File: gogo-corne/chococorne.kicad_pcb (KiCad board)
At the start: 2 copper layers, 112.9 x 97.1 mm, 40 parts, among them J1 MJ-4PP-9, SW10 SW_PUSH, SW11 SW_PUSH, SW12 SW_PUSH, SW14 SW_PUSH, SW15 SW_PUSH, SW16 SW_PUSH, SW17 SW_PUSH, SW18 SW_PUSH, SW19 SW_PUSH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

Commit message: the neatening
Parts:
- moved D6 4.07 mm to (149.1, 71.6)
- moved D18 4.07 mm to (149.1, 93.2)
- moved D12 4.07 mm to (149.1, 81.8)
- moved D5 1.55 mm to (149.1, 58.9)
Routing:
- net row3: track 115.5 -> 150.9 mm
- net col1: track 163.8 -> 156.1 mm
- net row1: track 120.8 -> 127.0 mm
- net Net-(D18-Pad2): track 23.6 -> 18.8 mm
- net Net-(D17-Pad2): track 35.4 -> 38.4 mm
- net Net-(D6-Pad2): track 21.4 -> 24.0 mm
- net Net-(D11-Pad2): track 35.4 -> 37.9 mm
- net row2: track 112.4 -> 113.8 mm
- net row0: track 126.8 -> 128.2 mm
- net Net-(D19-Pad2): track 51.6 -> 50.6 mm
- net col3: track 128.1 -> 127.5 mm
- net col4: track 115.7 -> 115.2 mm

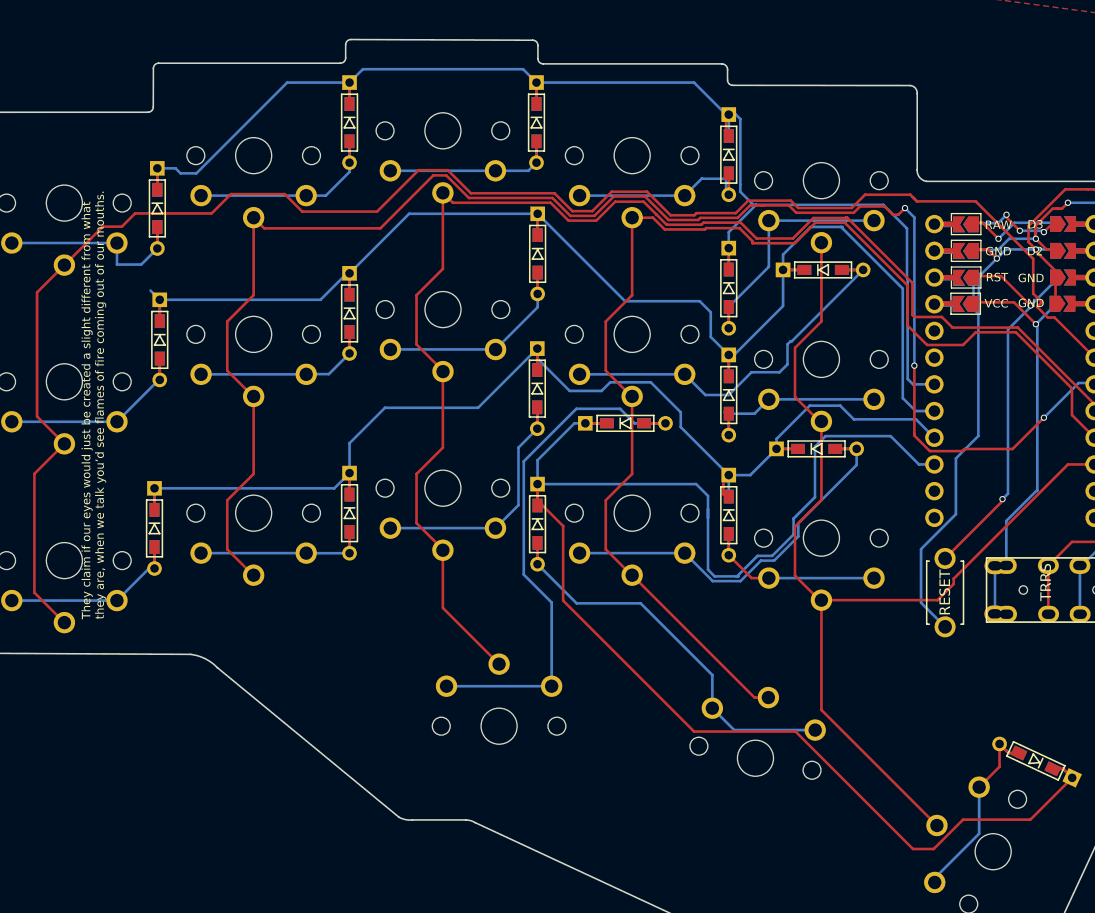
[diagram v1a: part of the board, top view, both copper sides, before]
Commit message: move some diodes
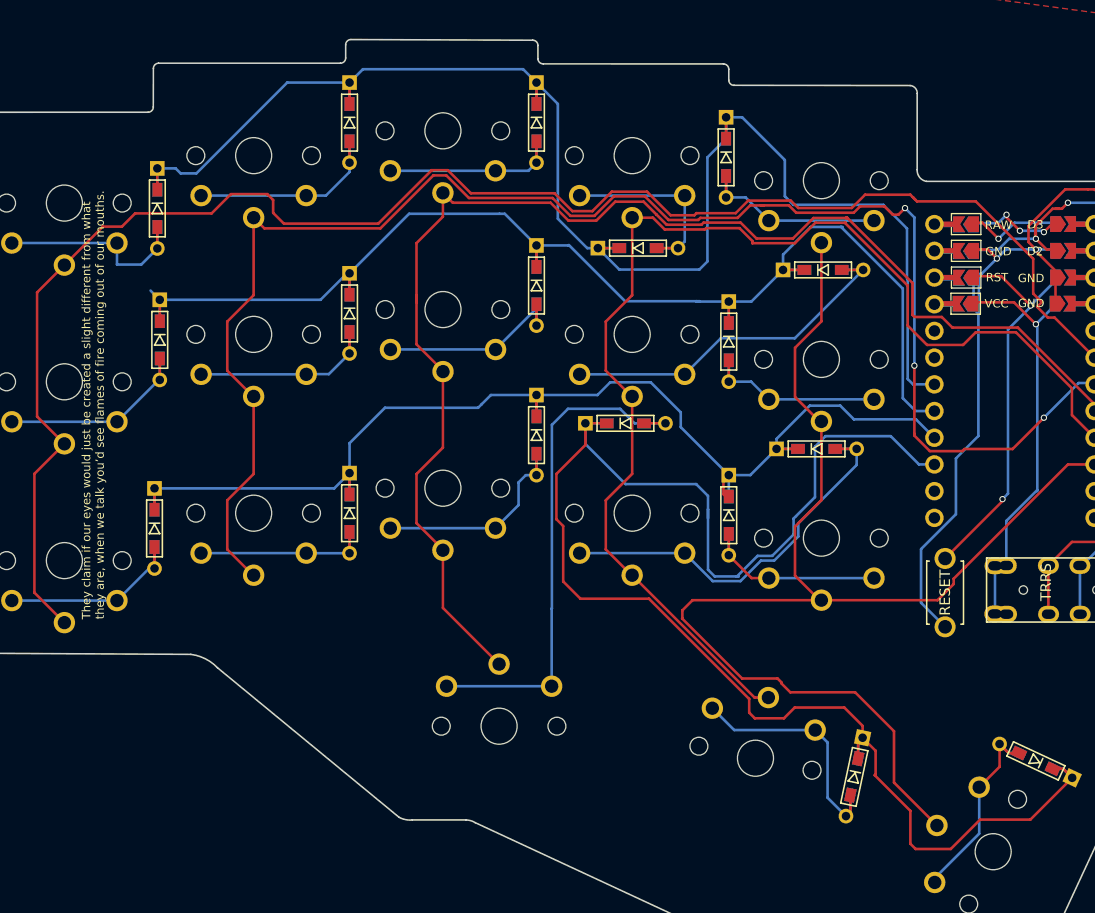
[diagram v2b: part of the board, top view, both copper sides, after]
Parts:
- moved D20 38.5 mm to (161.0, 118.1), turned to -102 degrees
- moved D6 12.4 mm to (148.8, 59.2)
- moved D5 12.4 mm to (140.5, 67.8), turned to 0 degrees
- moved D12 5.08 mm to (149.1, 76.7)
- moved D16 4.42 mm to (130.8, 85.6)
- moved D10 3.02 mm to (130.8, 71.4)
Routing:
- net col5: track 95.8 -> 119.5 mm
- net row0: track 128.2 -> 144.5 mm
- net Net-(D20-Pad2): track 38.9 -> 24.4 mm
- net row1: track 127.0 -> 119.8 mm
- net Net-(D6-Pad2): track 24.0 -> 19.2 mm
- net row2: track 113.8 -> 109.9 mm
- net Net-(D16-Pad2): track 25.2 -> 21.3 mm
- net Net-(D11-Pad2): track 37.9 -> 35.2 mm
- net Net-(D19-Pad2): track 50.6 -> 48.9 mm
- net col1: track 156.1 -> 157.8 mm
- net row3: track 150.9 -> 152.5 mm
- net Net-(D10-Pad2): track 21.0 -> 19.7 mm
- net Net-(D5-Pad2): track 18.6 -> 19.3 mm
- net col3: track 127.5 -> 128.1 mm
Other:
- outline, holes or cut-outs redrawn

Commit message: changes based on kyek's feedback
changes from @duckyb
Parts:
- SW10, SW11, SW12, SW14, SW15, SW16, SW17, SW18, SW19, SW2, SW3, SW4, SW5, SW6, SW8, SW9: footprint Kailh:SW_PG1350_rev_DPB2.2 -> Kailh:SW_PG1350_rev_DPB-mm
- moved D21 1.01 mm to (179.0, 115.8), turned to -25 degrees
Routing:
- net row3: track 152.5 -> 140.4 mm
- net Net-(D21-Pad2): track 20.1 -> 25.4 mm
- net col2: track 150.8 -> 152.5 mm
- net col1: track 157.8 -> 158.6 mm

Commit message: Fix DRC on gogo-corne
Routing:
- net col2: track 152.5 -> 142.1 mm
- net row1: track 119.8 -> 114.9 mm
- net row3: track 140.4 -> 136.0 mm
- net GND: track 113.2 -> 115.6 mm
- net Net-(D2-Pad2): track 20.6 -> 18.1 mm
- net row2: track 110.2 -> 112.2 mm
- net Net-(D19-Pad2): track 48.9 -> 50.0 mm
- net col5: track 119.5 -> 118.5 mm
- net col3: track 128.1 -> 127.0 mm
- net LED: track 9.33 -> 8.61 mm
- net Net-(D17-Pad2): track 38.4 -> 37.7 mm
- net reset: track 37.3 -> 36.9 mm, vias 2 -> 1
